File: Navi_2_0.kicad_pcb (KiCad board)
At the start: 4 copper layers, 101.7 x 148 mm, 117 parts, among them J1 USB_B_Micro, J10 BAT-, J2 Conn_01x24_Male, J23 Conn_01x06_Male, J27 Micro_SD_Card_Det, J8 SELECT, J9 BAT+, Q1 DMG2301L-7, Q2 Q_NMOS_GSD, Q3 DMG2301L-7, Q6 DMG2301L-7, SW1 SW_Push, SW2 SW_Push, SW3 WKUP, U1 MT3420C, U2 MT3420C, U3 ESP32-WROOM-32, U4 CH330N, U5 L96-M33, U6 LSM6DS3, U7 TCN75-3.3

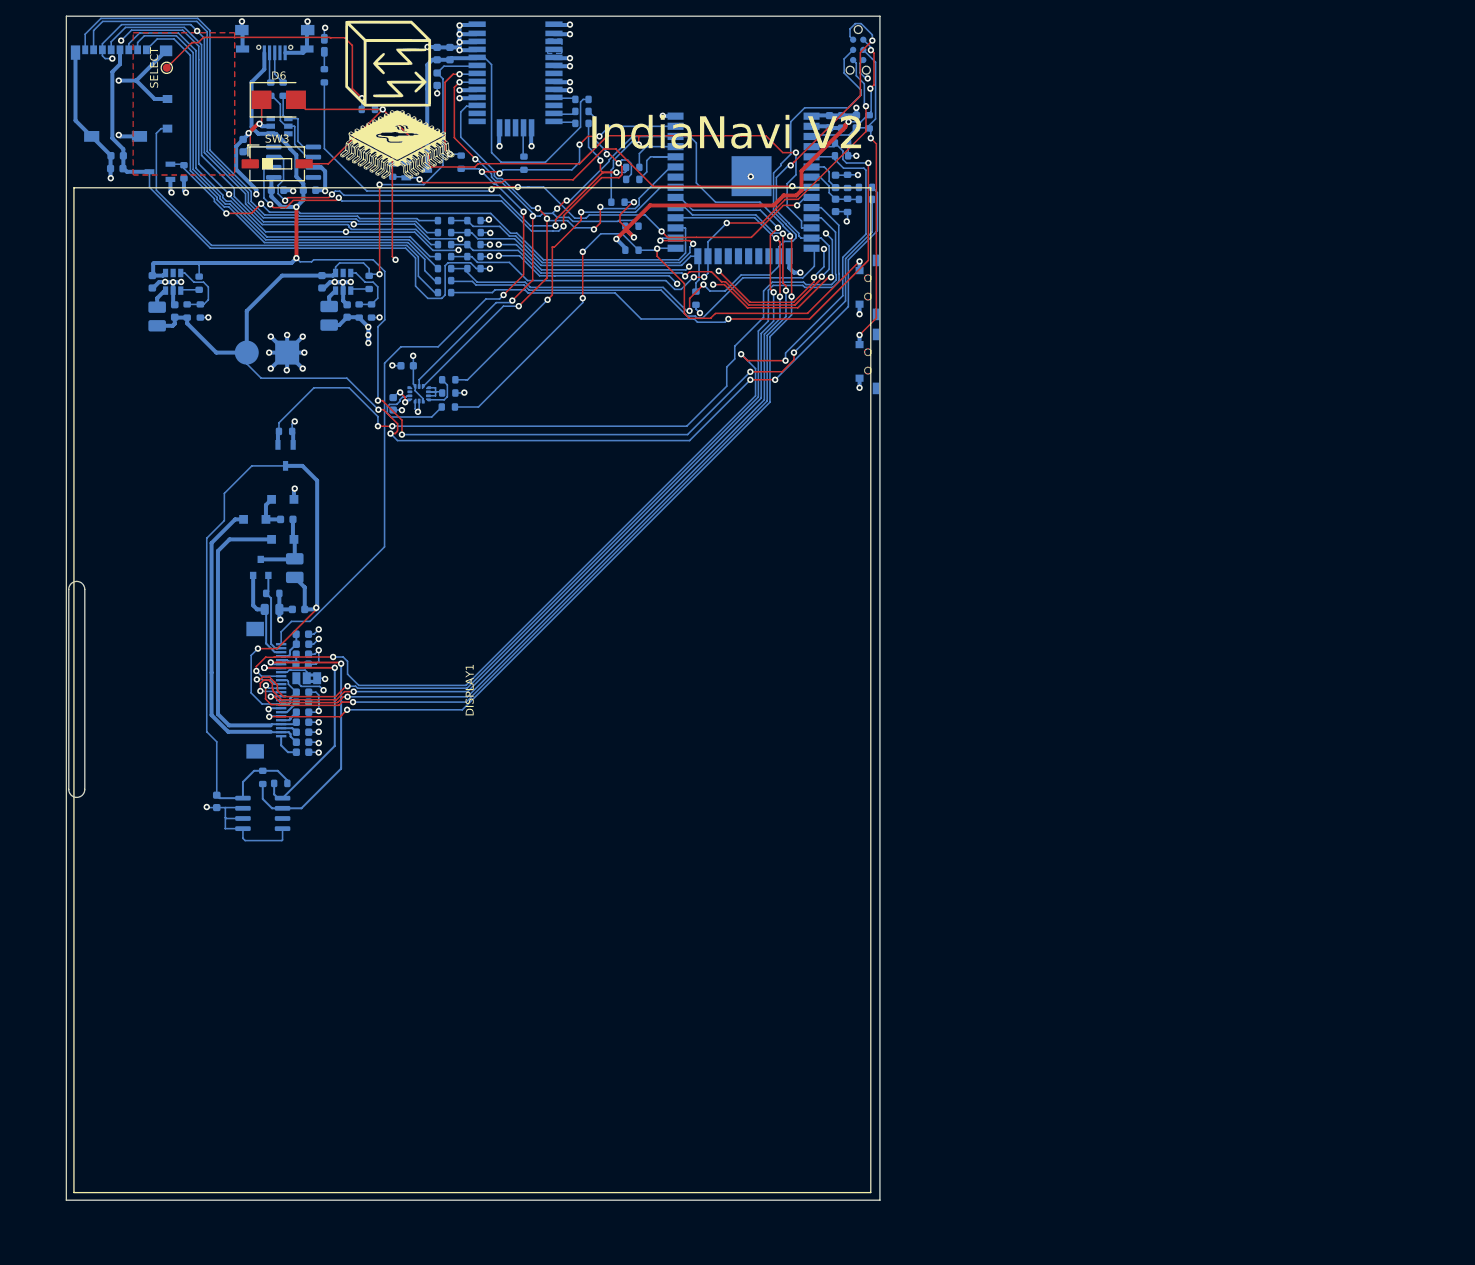
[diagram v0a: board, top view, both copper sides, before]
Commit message: Zwischenstand erste Platzierung
Es fehlen noch die Schaltregler und Reset / Programmierschaltung
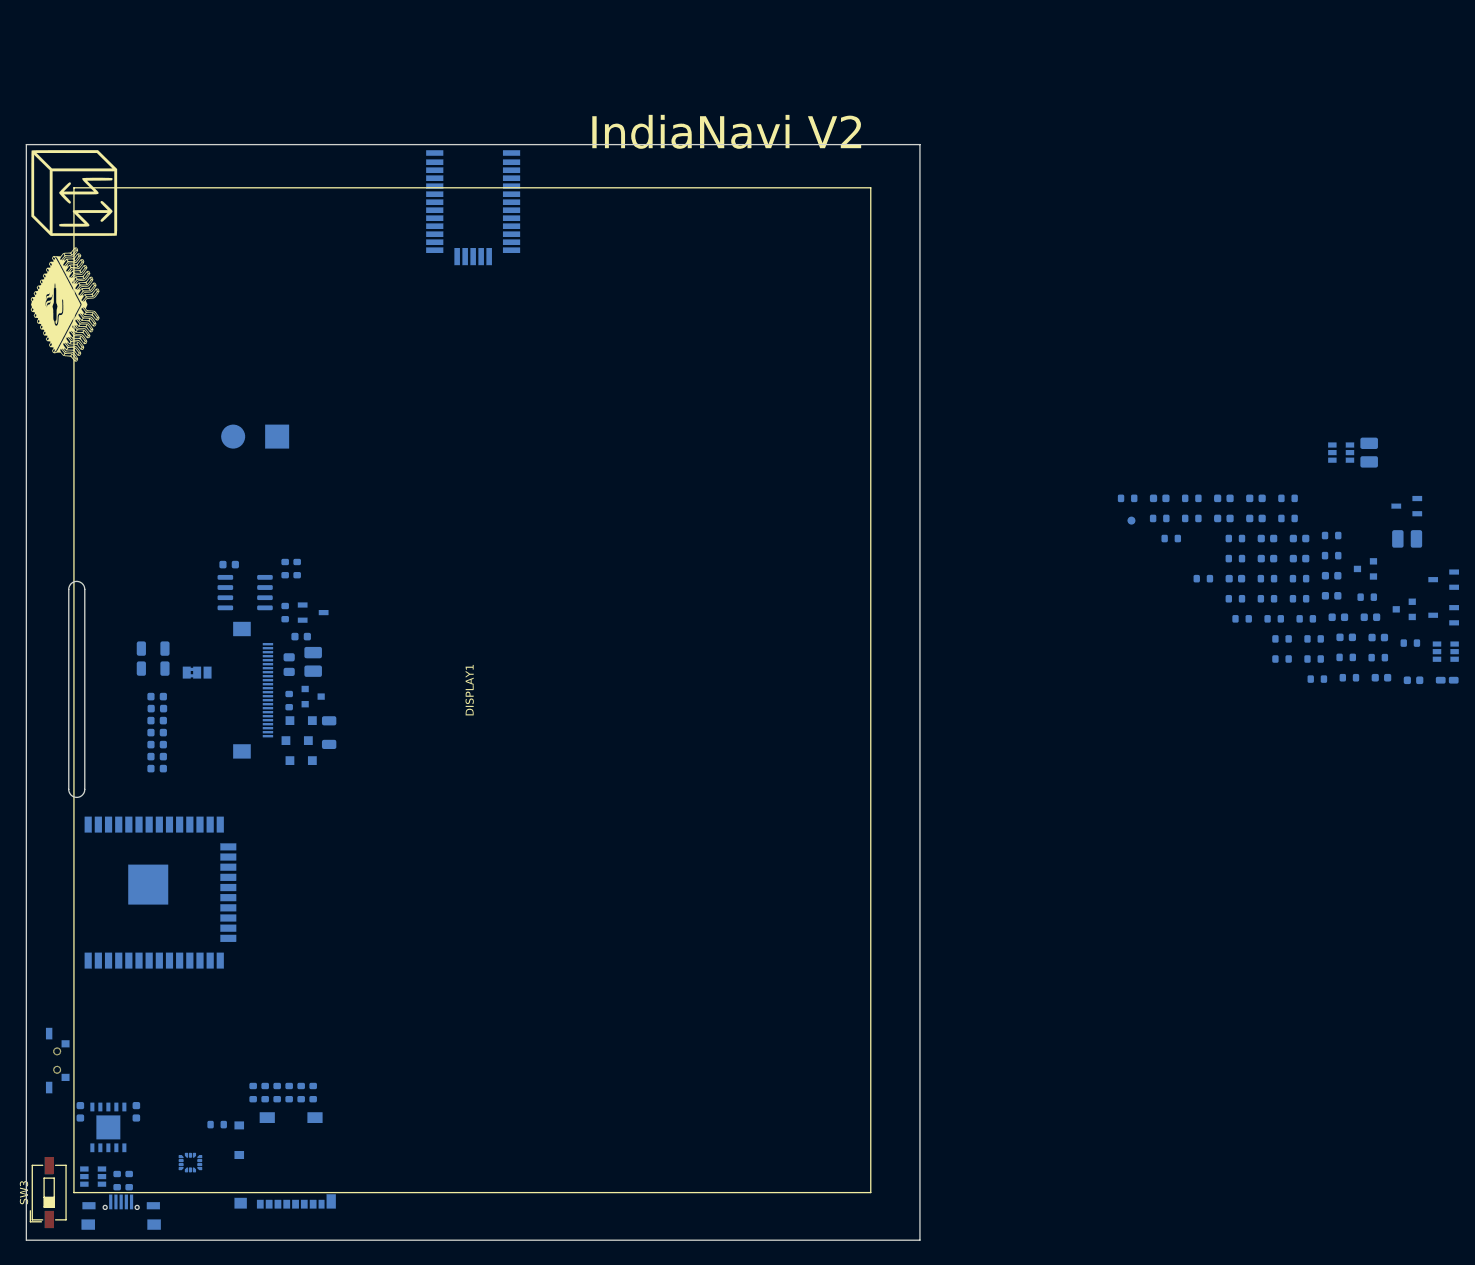
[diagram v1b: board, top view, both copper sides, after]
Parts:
- removed C23: 4µ7, Capacitor_SMD:C_0603_1608Metric
- removed D6: SFH 2240, Diode_SMD:D_SMB
- removed J23: Conn_01x06_Male, Connector:Tag-Connect_TC2030-IDC-NL_2x03_P1.27mm_Vertical
- removed R24, R25, R26, R48, R49: 10R, Resistor_SMD:R_0603_1608Metric
- removed R50: 100K, Resistor_SMD:R_0603_1608Metric
- removed SW2: SW_Push, Navi_2_0:TS36CA
- added Q4: Q_NPN_BEC, Package_TO_SOT_SMD:SOT-23, B.Cu at (205.9, 105.1)
- added Q5: Q_NPN_BEC, Package_TO_SOT_SMD:SOT-23, B.Cu at (201.0, 100.0)
- added Q7: DMG2301L-7, Package_TO_SOT_SMD:TSOT-23, B.Cu at (210.8, 105.8)
- C13, C24, C25: footprint Capacitor_SMD:C_0603_1608Metric -> Capacitor_SMD:C_1206_3216Metric
- C20: value 4µ7 -> 100n
- D3, D4, D5: value D -> MBR340F
- J8: moved to B.Cu
- L1, L2, L3: value 2.2µ -> 4µ7
- Q2: value Q_NMOS_GSD -> TF2310
- R19, R20: value 10R -> 4K7
- R23: value 10R -> 100K
- U4: value CH330N -> CH340K; footprint Package_SO:SOIC-8_3.9x4.9mm_P1.27mm -> Package_SO:SSOP-10_EP1_3.9x4.9mm_P1.00mm
- moved Q6 168.4 mm to (210.8, 101.4)
- moved C19 164.5 mm to (198.6, 108.6), turned to 180 degrees
- moved D2 161.2 mm to (211.3, 114.0), turned to 180 degrees
- moved R10 155.1 mm to (202.6, 111.1), turned to 180 degrees
- moved C6 154.7 mm to (207.0, 114.0)
- moved L1 152.5 mm to (201.5, 85.5), turned to 90 degrees
- moved R33 150.5 mm to (196.8, 95.9), turned to 180 degrees
- moved C18 149.4 mm to (187.3, 93.7)
- moved U1 147.6 mm to (198.0, 85.5), turned to 180 degrees
- moved J1 146.8 mm to (45.5, 180.1), turned to 180 degrees
- moved U2 145.4 mm to (211.1, 110.4), turned to 180 degrees
- moved R2 142.4 mm to (192.8, 101.3), turned to 180 degrees
- moved R4 138.0 mm to (45.0, 176.5), turned to 90 degrees
- moved R3 137.7 mm to (206.6, 109.3), turned to 180 degrees
- moved L2 137.6 mm to (206.2, 96.3), turned to 180 degrees
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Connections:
- net JTAG_TMS renamed SD_CLK
- C24 pad 1: Net-(C23-Pad1) -> GND
- C24 pad 2: GND -> Net-(C24-Pad2)
- C25 pad 1: Net-(C20-Pad1) -> GND
- C25 pad 2: GND -> Net-(C25-Pad2)
- C9 pad 1: Net-(C9-Pad1) -> +5V
- D1 pad 3: no_connect_(D1-Pad3) -> unconnected-(D1-Pad3)
- D1 pad 6: no_connect_(D1-Pad6) -> unconnected-(D1-Pad6)
- J1 pad 4: no_connect_(J1-Pad4) -> unconnected-(J1-Pad4)
- J2 pad 20: Net-(C20-Pad1) -> Net-(C25-Pad2)
- J2 pad 21: Net-(C23-Pad1) -> Net-(C24-Pad2)
- J2 pad 24: EINK_EEPROM_~EN -> unconnected-(J2-Pad24)
- J2 pad 6: EINK_SPI_MISO -> unconnected-(J2-Pad6)
- R16 pad 1: G_INT2 -> I2C_DAT
- R19 pad 1: Net-(R19-Pad1) -> Net-(Q4-Pad1)
- R19 pad 2: UART1_RX -> Net-(Q5-Pad2)
- R20 pad 1: Net-(R20-Pad1) -> Net-(Q5-Pad1)
- R20 pad 2: UART1_TX -> Net-(Q4-Pad2)
- R21 pad 2: EINK_SPI_MISO -> I2C_CLK
- R23 pad 1: UART1_RX -> Net-(J27-Pad10)
- R23 pad 2: Net-(R23-Pad2) -> Net-(C18-Pad1)
- R35 pad 1: JTAG_TCK -> Net-(Q7-Pad3)
- R35 pad 2: Net-(C18-Pad1) -> SD_DAT0
- R36 pad 1: JTAG_TDO -> SD_DAT3
- R37 pad 1: SD_DAT0 -> SD_nCS
- R40 pad 1: IO27 -> Net-(R40-Pad1)
- R42 pad 1: JTAG_TCK -> SD_DAT3
- R43 pad 1: JTAG_TDO -> SD_nCS
- U1 pad 5: no_connect_(U1-Pad5) -> unconnected-(U1-Pad5)
- U2 pad 5: no_connect_(U2-Pad5) -> unconnected-(U2-Pad5)
- U3 pad 12: IO27 -> Net-(R40-Pad1)
- U3 pad 16: JTAG_TCK -> SD_DAT3
- U3 pad 17: no_connect_(U3-Pad17) -> unconnected-(U3-Pad17)
- U3 pad 18: no_connect_(U3-Pad18) -> unconnected-(U3-Pad18)
- U3 pad 19: no_connect_(U3-Pad19) -> unconnected-(U3-Pad19)
- U3 pad 20: no_connect_(U3-Pad20) -> unconnected-(U3-Pad20)
- U3 pad 21: no_connect_(U3-Pad21) -> unconnected-(U3-Pad21)
- U3 pad 22: no_connect_(U3-Pad22) -> unconnected-(U3-Pad22)
- U3 pad 23: JTAG_TDO -> SD_nCS
- U3 pad 25: G_INT2 -> I2C_DAT
- U3 pad 31: G_INT1 -> UART_GPS_RX
- U3 pad 32: no_connect_(U3-Pad32) -> unconnected-(U3-Pad32)
- U3 pad 33: I2C_DAT -> G_INT1
- U3 pad 34: Net-(R20-Pad1) -> UART1_TX
- U3 pad 35: Net-(R19-Pad1) -> UART1_RX
- U3 pad 36: EINK_SPI_MISO -> I2C_CLK
- U3 pad 37: EINK_EEPROM_~EN -> UART_GPS_TX
- U4 pad 4: no_connect_(U4-Pad4) -> Net-(Q5-Pad2)
- U4 pad 5: +5V -> unconnected-(U4-Pad5)
- U4 pad 6: UART1_TX -> Net-(Q4-Pad2)
- U4 pad 7: UART1_RX -> +5V
- U4 pad 8: Net-(C9-Pad1) -> UART1_TX
- U5 pad 2: no_connect_(U5-Pad2) -> unconnected-(U5-Pad2)
- U5 pad 20: no_connect_(U5-Pad20) -> unconnected-(U5-Pad20)
- U5 pad 24: no_connect_(U5-Pad24) -> unconnected-(U5-Pad24)
- U5 pad 25: Net-(R24-Pad2) -> UART_GPS_RX
- U5 pad 26: Net-(R23-Pad2) -> UART_GPS_TX
- U5 pad 28: Net-(R25-Pad2) -> unconnected-(U5-Pad28)
- U5 pad 29: no_connect_(U5-Pad29) -> unconnected-(U5-Pad29)
- U5 pad 3: I2C_DAT -> unconnected-(U5-Pad3)
- U5 pad 30: no_connect_(U5-Pad30) -> unconnected-(U5-Pad30)
- U5 pad 6: EINK_SPI_MISO -> unconnected-(U5-Pad6)
- U5 pad 7: Net-(R26-Pad2) -> unconnected-(U5-Pad7)
- U6 pad 10: no_connect_(U6-Pad10) -> unconnected-(U6-Pad10)
- U6 pad 11: no_connect_(U6-Pad11) -> unconnected-(U6-Pad11)
- U6 pad 13: EINK_SPI_MISO -> I2C_CLK
- U6 pad 4: Net-(U6-Pad4) -> G_INT1
- U6 pad 9: Net-(U6-Pad9) -> unconnected-(U6-Pad9)
- U7 pad 3: no_connect_(U7-Pad3) -> unconnected-(U7-Pad3)
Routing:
- net GND: track 449.5 -> 0.00 mm, vias 88 -> 0
- net EINK_SPI_MISO: track 210.6 -> 0.00 mm, vias 10 -> 0
- net +BATT: track 184.2 -> 0.00 mm, vias 6 -> 0
- net +5V: track 172.2 -> 0.00 mm, vias 6 -> 0
- net EINK_STATE: track 131.9 -> 0.00 mm, vias 4 -> 0
- net EINK_SPI_CLK: track 120.4 -> 0.00 mm, vias 4 -> 0
- net EINK_~CS: track 119.4 -> 0.00 mm, vias 4 -> 0
- net EINK_DC: track 117.9 -> 0.00 mm, vias 2 -> 0
- net EINK_VCC: track 114.0 -> 0.00 mm, vias 2 -> 0
- net EINK_SPI_MOSI: track 113.9 -> 0.00 mm, vias 4 -> 0
- net +3V3: track 113.0 -> 0.00 mm, vias 19 -> 0
- net EINK_EEPROM_~EN: track 109.7 -> 0.00 mm, vias 6 -> 0
- net IO27: track 105.4 -> 0.00 mm, vias 3 -> 0
- net EINK_VCC_~EN: track 98.8 -> 0.00 mm, vias 2 -> 0
- net SD_CLK: track 96.6 -> 0.00 mm, vias 4 -> 0
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- removed copper zone on F.Cu, net Net-(J8-Pad1)
- removed copper zone on B.Cu, net Net-(U5-Pad16)
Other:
- board size 101.7 x 148 mm -> 111.7 x 136.9 mm
- board text removed: "BAT+"
- board text removed: "BAT-"
- board text removed: "BOOT"
- board text removed: "RESET"

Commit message: Update G-Sensor
#9 Ersetzt mit lsm303ah
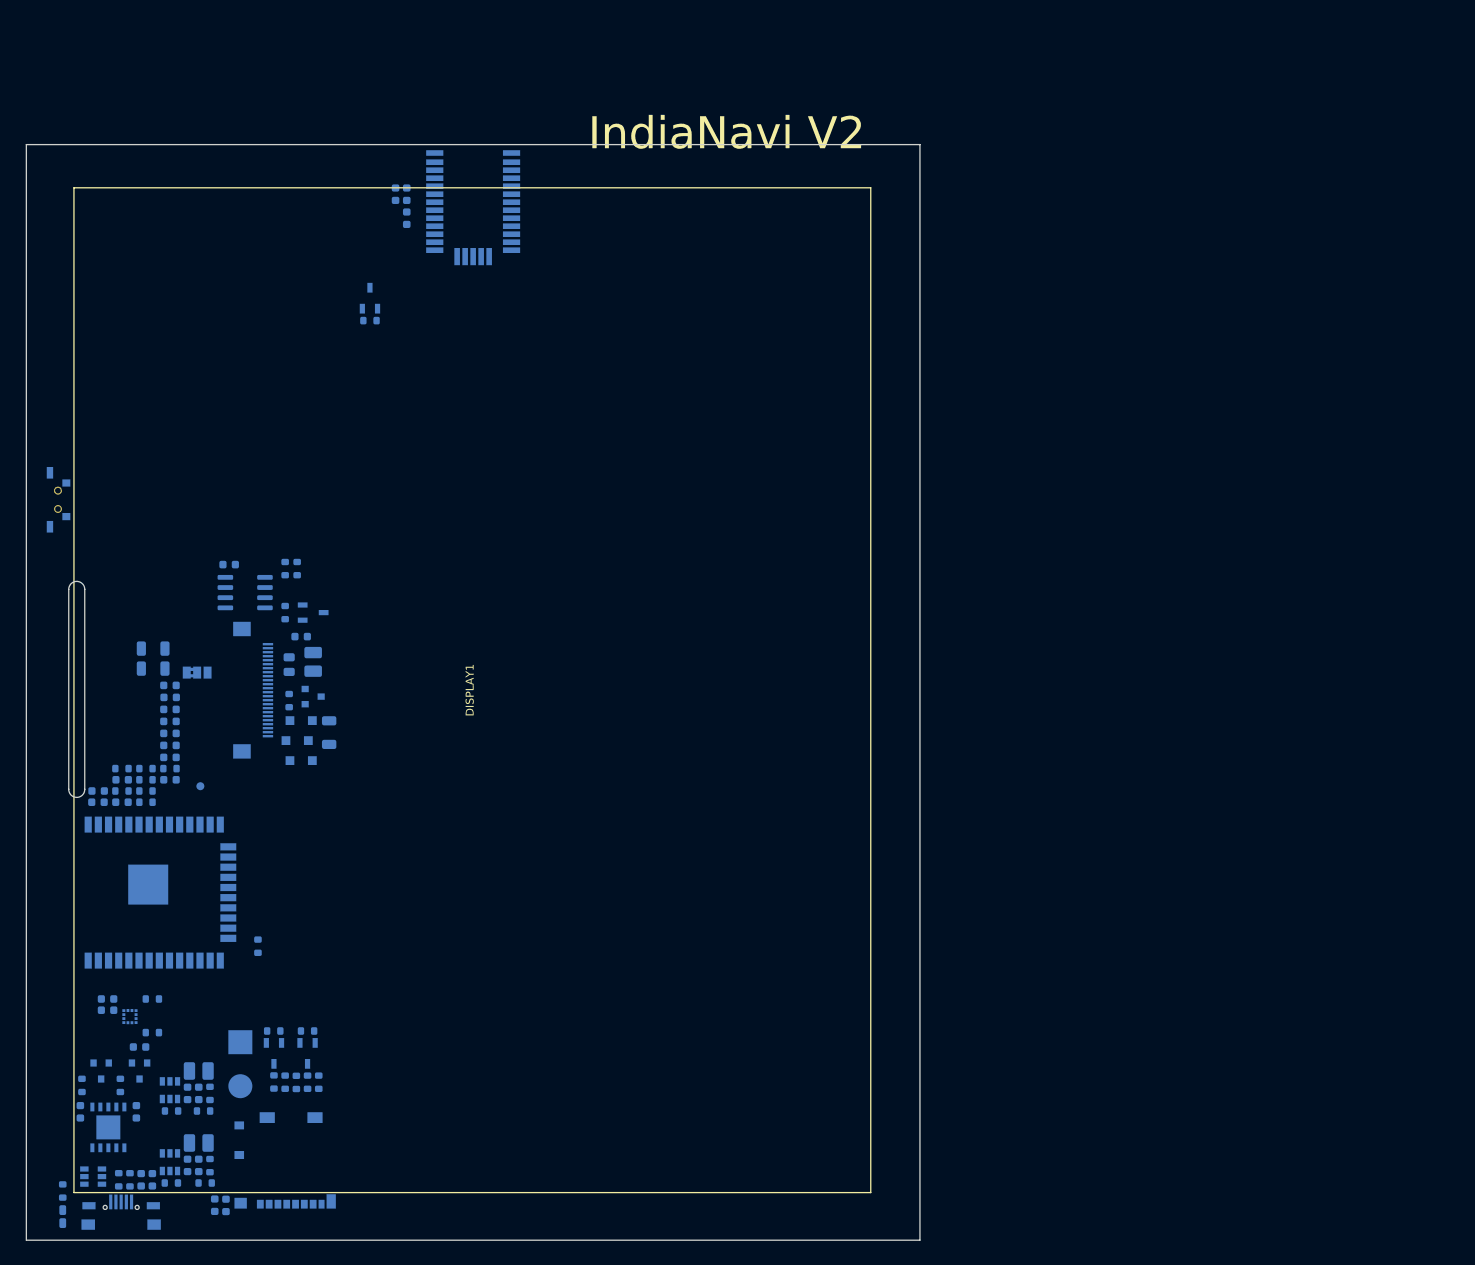
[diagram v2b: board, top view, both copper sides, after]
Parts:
- removed G***: LOGO, KiCad:Symbol_kurzschlussblog_12mm
- removed G***: LOGO, Kicad:Platinenmacher_14
- removed R22, R34, R40, R41, R42, R43, R44, R45, R46, R47: 10R, Resistor_SMD:R_0603_1608Metric
- removed SW3: WKUP, Button_Switch_SMD:SW_DIP_SPSTx01_Slide_6.7x4.1mm_W6.73mm_P2.54mm_LowProfile_JPin
- added C23: 220n, Capacitor_SMD:C_0603_1608Metric, B.Cu at (43.8, 153.8)
- C12, C15, C17, C18, C20, C26, C4, C5, C6, C8, C9: value 100n -> 220n
- U6: value LSM6DS3 -> LSM303AH; footprint Package_LGA:LGA-14_3x2.5mm_P0.5mm_LayoutBorder3x4y -> Package_LGA:LGA-12_2x2mm_P0.5mm
- moved D2 185.6 mm to (38.2, 181.0), turned to 90 degrees
- moved R18 175.9 mm to (38.2, 177.8), turned to 90 degrees
- moved U1 171.2 mm to (51.6, 174.2), turned to -90 degrees
- moved C6 170.9 mm to (48.0, 176.4), turned to -90 degrees
- moved Q5 170.0 mm to (43.0, 162.8), turned to -90 degrees
- moved L1 169.9 mm to (55.2, 171.8), turned to 0 degrees
- moved U2 168.6 mm to (51.6, 165.2), turned to -90 degrees
- moved Q4 168.3 mm to (47.8, 162.8), turned to -90 degrees
- moved R3 165.5 mm to (51.8, 167.8), turned to 0 degrees
- moved L2 165.0 mm to (55.2, 162.8), turned to 0 degrees
- moved C7 160.8 mm to (49.4, 176.4), turned to -90 degrees
- moved C5 160.7 mm to (42.6, 129.2)
- moved R2 160.0 mm to (51.8, 176.8), turned to 0 degrees
- moved C15 159.3 mm to (47.8, 159.8), turned to 0 degrees
- moved R10 159.2 mm to (56.6, 174.6), turned to -90 degrees
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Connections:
- C14 pad 1: +3V3 -> GND
- C14 pad 2: GND -> +3V3
- C15 pad 1: GND -> Net-(C15-Pad1)
- C15 pad 2: +3V3 -> GND
- J27 pad 1: Net-(J27-Pad1) -> SD_DAT2
- J27 pad 10: Net-(J27-Pad10) -> SD_nDET
- J27 pad 2: Net-(J27-Pad2) -> SD_DAT3
- J27 pad 3: Net-(J27-Pad3) -> SD_nCS
- J27 pad 5: Net-(J27-Pad5) -> SD_CLK
- J27 pad 7: Net-(J27-Pad7) -> SD_DAT0
- J27 pad 8: Net-(J27-Pad8) -> SD_DAT1
- J8 pad 1: Net-(J8-Pad1) -> Net-(U3-Pad12)
- Q7 pad 1: Net-(J27-Pad10) -> SD_nDET
- R23 pad 1: Net-(J27-Pad10) -> SD_nDET
- U3 pad 12: Net-(R40-Pad1) -> Net-(U3-Pad12)
- U5 pad 23: Net-(R22-Pad2) -> GPS_SUPPLY
- U6 pad 1: Net-(R34-Pad2) -> I2C_CLK
- U6 pad 10: unconnected-(U6-Pad10) -> +3V3
- U6 pad 12: +3V3 -> G_INT1
- U6 pad 2: Net-(R34-Pad2) -> +3V3
- U6 pad 3: Net-(R34-Pad2) -> unconnected-(U6-Pad3)
- U6 pad 4: G_INT1 -> I2C_DAT
- U6 pad 5: +3V3 -> Net-(C15-Pad1)
- U6 pad 7: GND -> unconnected-(U6-Pad7)
- U6 pad 8: +3V3 -> GND
- U6 pad 9: unconnected-(U6-Pad9) -> +3V3

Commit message: Commit vor Routing
Sicherheitscommit vor routing
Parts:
- removed J8: SELECT, TestPoint:TestPoint_Pad_D1.0mm
- added SW2: SW_Push, Button_Switch_SMD:SW_DIP_SPSTx01_Slide_Copal_CHS-01B_W7.62mm_P1.27mm, F.Cu at (35.6, 168.8)
- SW1: footprint Navi_2_0:TS36CA -> Button_Switch_SMD:SW_DIP_SPSTx01_Slide_Copal_CHS-01B_W7.62mm_P1.27mm
- moved SW1 40.5 mm to (59.6, 125.4)
- moved C24 8.10 mm to (52.0, 102.3)
- moved C25 8.10 mm to (52.0, 104.8)

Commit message: Angefangen zu routen.
Erstes Routing gestertet. klärung der frage #10
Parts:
- moved R16 1.52 mm to (48.0, 158.6)
- moved R21 1.46 mm to (48.0, 153.4)
- moved R10 1.40 mm to (58.0, 174.6)
- moved C26 1.40 mm to (51.6, 113.2)
- moved JP1 1.35 mm to (56.0, 112.1), turned to 90 degrees
- moved C27 1.30 mm to (51.6, 114.8)
- moved C10 1.20 mm to (56.4, 174.6)
- moved C28 1.20 mm to (51.6, 116.4)
- moved C21 1.10 mm to (51.6, 118.0)
- moved L1 1.02 mm to (56.2, 171.6)
- moved C1 1.00 mm to (54.8, 174.6)
- moved C22 1.00 mm to (51.6, 119.6)
- moved C29 0.90 mm to (51.6, 121.2)
- moved SW1 0.85 mm to (60.2, 126.0)
- moved C30 0.80 mm to (51.6, 122.8)
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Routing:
- net SD_DAT2: track 0.00 -> 55.6 mm
- net Net-(C18-Pad1): track 0.00 -> 41.5 mm
- net SD_DAT1: track 0.00 -> 16.2 mm
- net SD_DAT3: track 0.00 -> 15.8 mm
- net SD_DAT0: track 0.00 -> 15.5 mm
- net SD_nCS: track 0.00 -> 14.7 mm
- net SD_CLK: track 0.00 -> 14.4 mm
- net Net-(C13-Pad1): track 0.00 -> 2.11 mm
- net Net-(Q7-Pad3): track 0.00 -> 1.75 mm
- net SD_nDET: track 0.00 -> 1.74 mm
